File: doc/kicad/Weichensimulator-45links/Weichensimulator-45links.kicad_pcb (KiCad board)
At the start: 2 copper layers, 38.1 x 38.1 mm, 9 parts, among them J1 Conn_01x02_Male, J2 Power, J3 Conn_01x02_Male, K1 HFD2_005-S-L2-D

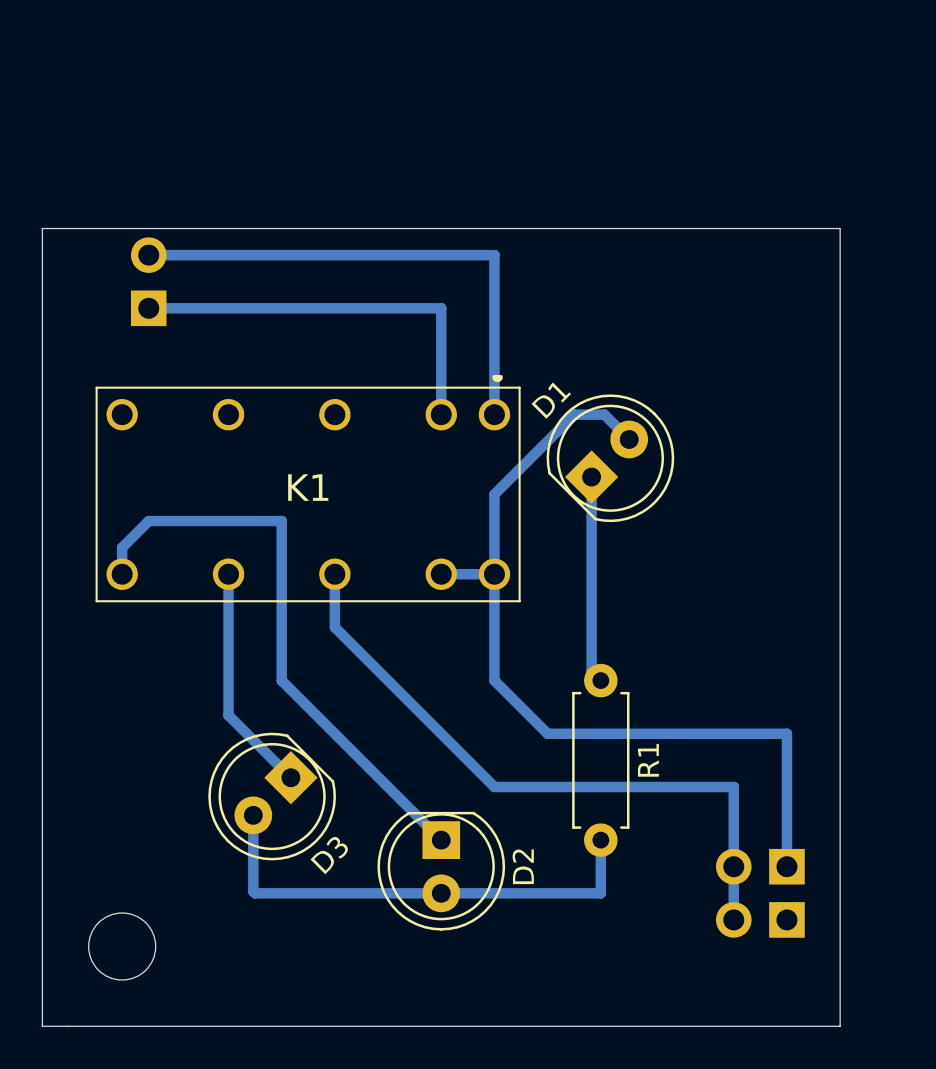
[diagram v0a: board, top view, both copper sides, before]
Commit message: Ecken rund gemacht, alle mit Montagelöcher
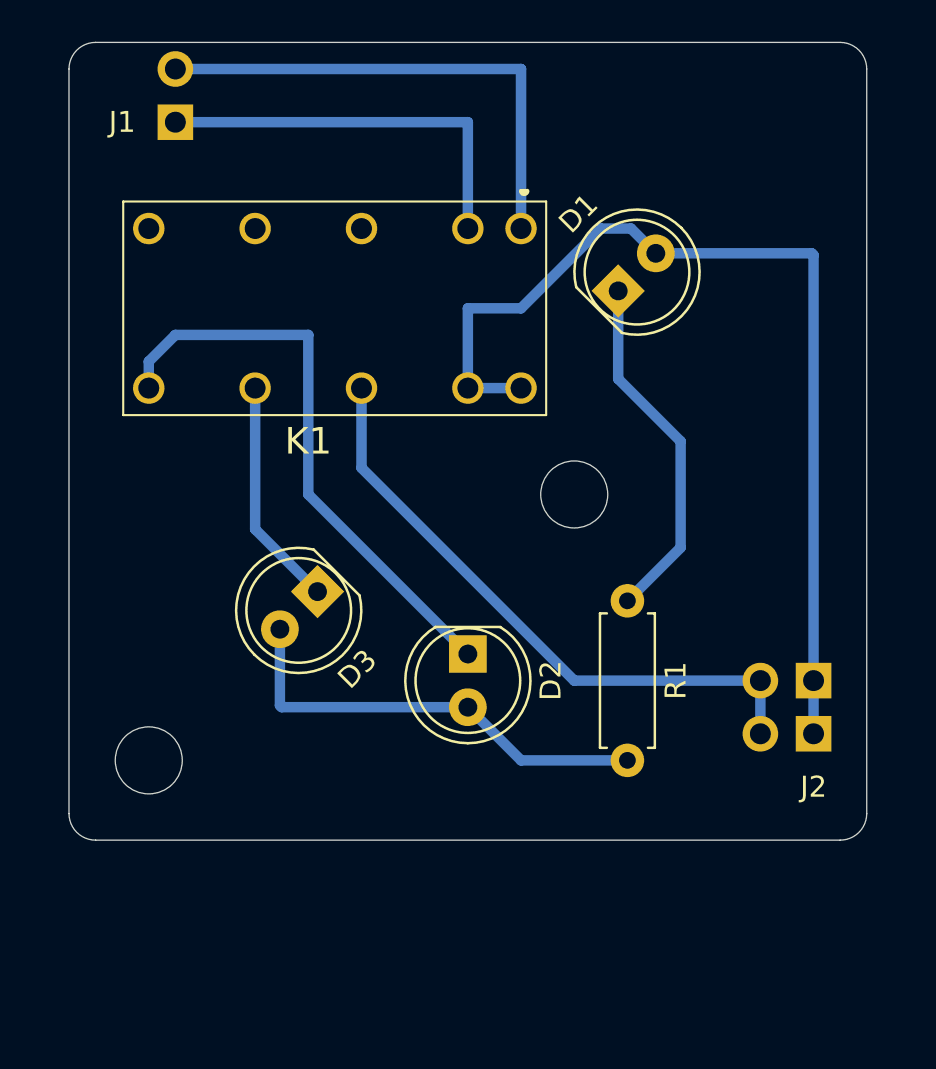
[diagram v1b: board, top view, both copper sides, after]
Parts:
- removed the H1 at (133.3, 130.8)
- added H1: MountingHole, Mounting_Holes:MountingHole_3.2mm_M3, F.Cu at (154.9, 109.2)
- added H1: MountingHole, Mounting_Holes:MountingHole_3.2mm_M3, F.Cu at (134.6, 121.9)
- moved D2 8.98 mm to (149.9, 116.8)
- moved D3 8.98 mm to (142.7, 113.9)
- moved J2 8.98 mm to (166.4, 118.1)
- moved K1 8.98 mm to (152.4, 96.5)
- moved D1 8.98 mm to (157.0, 99.5)
- moved J1 8.98 mm to (135.9, 91.4)
- moved J3 8.98 mm to (166.4, 120.7)
- moved R1 4.02 mm to (157.5, 114.3)
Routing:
- net Net-(D1-Pad1): track 9.90 -> 17.1 mm
- net +5V: track 41.3 -> 47.8 mm
- net Net-(D2-Pad2): track 22.8 -> 21.3 mm
- net GND: track 31.1 -> 29.6 mm
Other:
- outline, holes or cut-outs redrawn
- board text added: "©H3-H5N6 2021 Weiche li/45° v1.0"

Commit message: Platinen, die an jlcpcb geschickt worden sind.
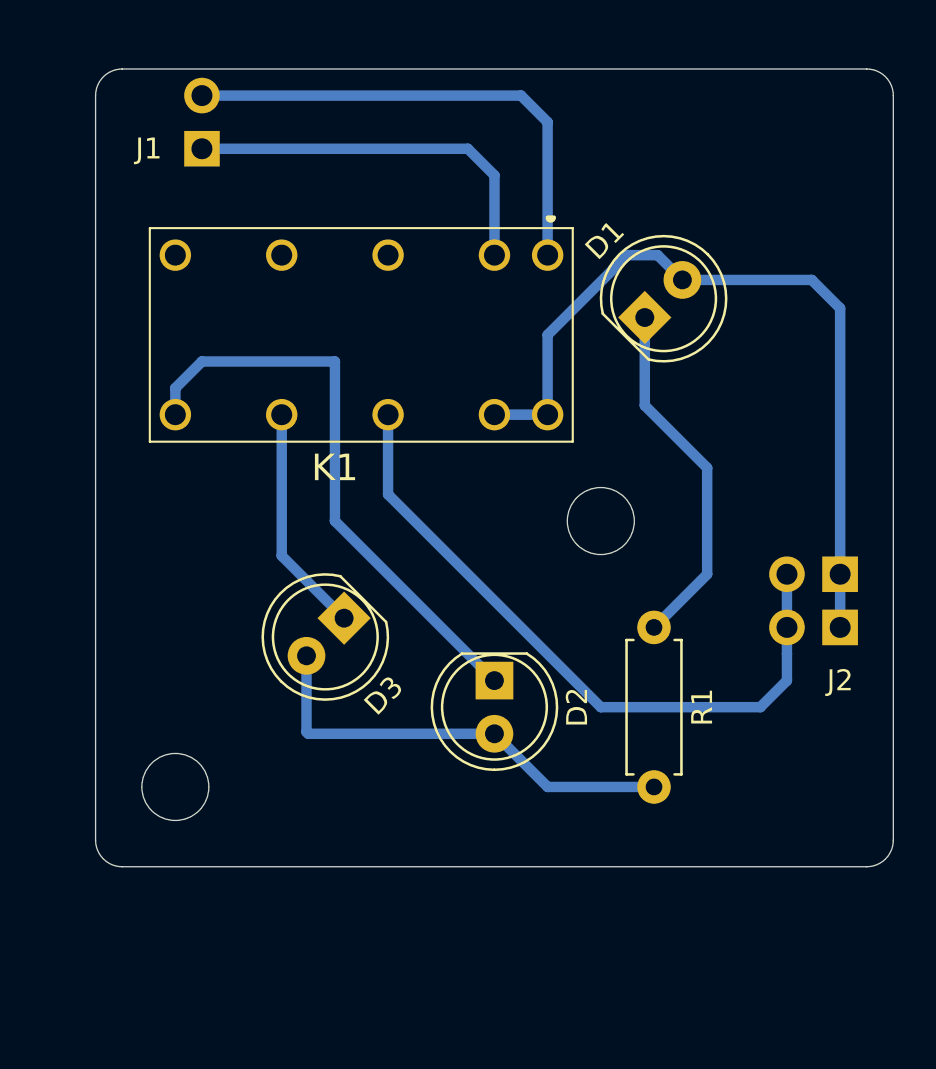
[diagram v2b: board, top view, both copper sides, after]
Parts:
- removed the H1 at (154.9, 109.2)
- removed the H1 at (134.6, 121.9)
- added H1: MountingHole, Mounting_Holes:MountingHole_3.2mm_M3, F.Cu at (156.2, 110.5)
- added H1: MountingHole, Mounting_Holes:MountingHole_3.2mm_M3, F.Cu at (135.9, 123.2)
- moved J3 5.24 mm to (167.6, 115.6)
- moved J2 5.24 mm to (167.6, 113.0)
- moved D1 1.80 mm to (158.3, 100.8)
- moved J1 1.80 mm to (137.2, 92.7)
- moved R1 1.80 mm to (158.8, 115.6)
- moved K1 1.80 mm to (153.7, 97.8)
- moved D2 1.80 mm to (151.1, 118.1)
- moved D3 1.80 mm to (143.9, 115.1)
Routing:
- net +5V: track 47.8 -> 38.2 mm
- net GND: track 29.6 -> 32.7 mm
- net Net-(J1-Pad1): track 19.1 -> 18.3 mm
- net Net-(J1-Pad2): track 24.1 -> 23.4 mm
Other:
- board text added: "+5V"
- board text added: "A"
- board text added: "G"
- board text added: "GND"

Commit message: Bezeichung auf der Bestückungsseite
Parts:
- K1: moved to B.Cu
- moved K1 7.62 mm to (153.7, 105.4)
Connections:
- K1 pad 1: Net-(J1-Pad2) -> +5V
- K1 pad 11: Net-(D3-Pad1) -> (no net)
- K1 pad 13: GND -> (no net)
- K1 pad 15: +5V -> Net-(J1-Pad1)
- K1 pad 16: +5V -> Net-(J1-Pad2)
- K1 pad 2: Net-(J1-Pad1) -> +5V
- K1 pad 4: (no net) -> GND
- K1 pad 6: (no net) -> Net-(D3-Pad1)
- K1 pad 8: (no net) -> Net-(D2-Pad1)
- K1 pad 9: Net-(D2-Pad1) -> (no net)
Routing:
- net Net-(D2-Pad2): track 21.3 -> 20.6 mm
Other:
- board text added: "©H3-H5N6 2021 Weiche li/45° v2.0"
- board text removed: "©H3-H5N6 2021 Weiche li/45° v1.0"

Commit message: Dateien aufgeräumt
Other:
- net class Default removed

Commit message: Kosmetik
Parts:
- K1: footprint HFD2005SL2D -> HongFa:HFD2005SL2D
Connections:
- K1 pad 11: (no net) -> unconnected-(K1-Pad11)
- K1 pad 13: (no net) -> unconnected-(K1-Pad13)
- K1 pad 9: (no net) -> unconnected-(K1-Pad9)
